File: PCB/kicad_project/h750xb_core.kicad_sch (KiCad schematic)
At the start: 9 parts, among them Q1 Q_NMOS_GSD, SW1 SW_DPST, SW2 SW_DPST

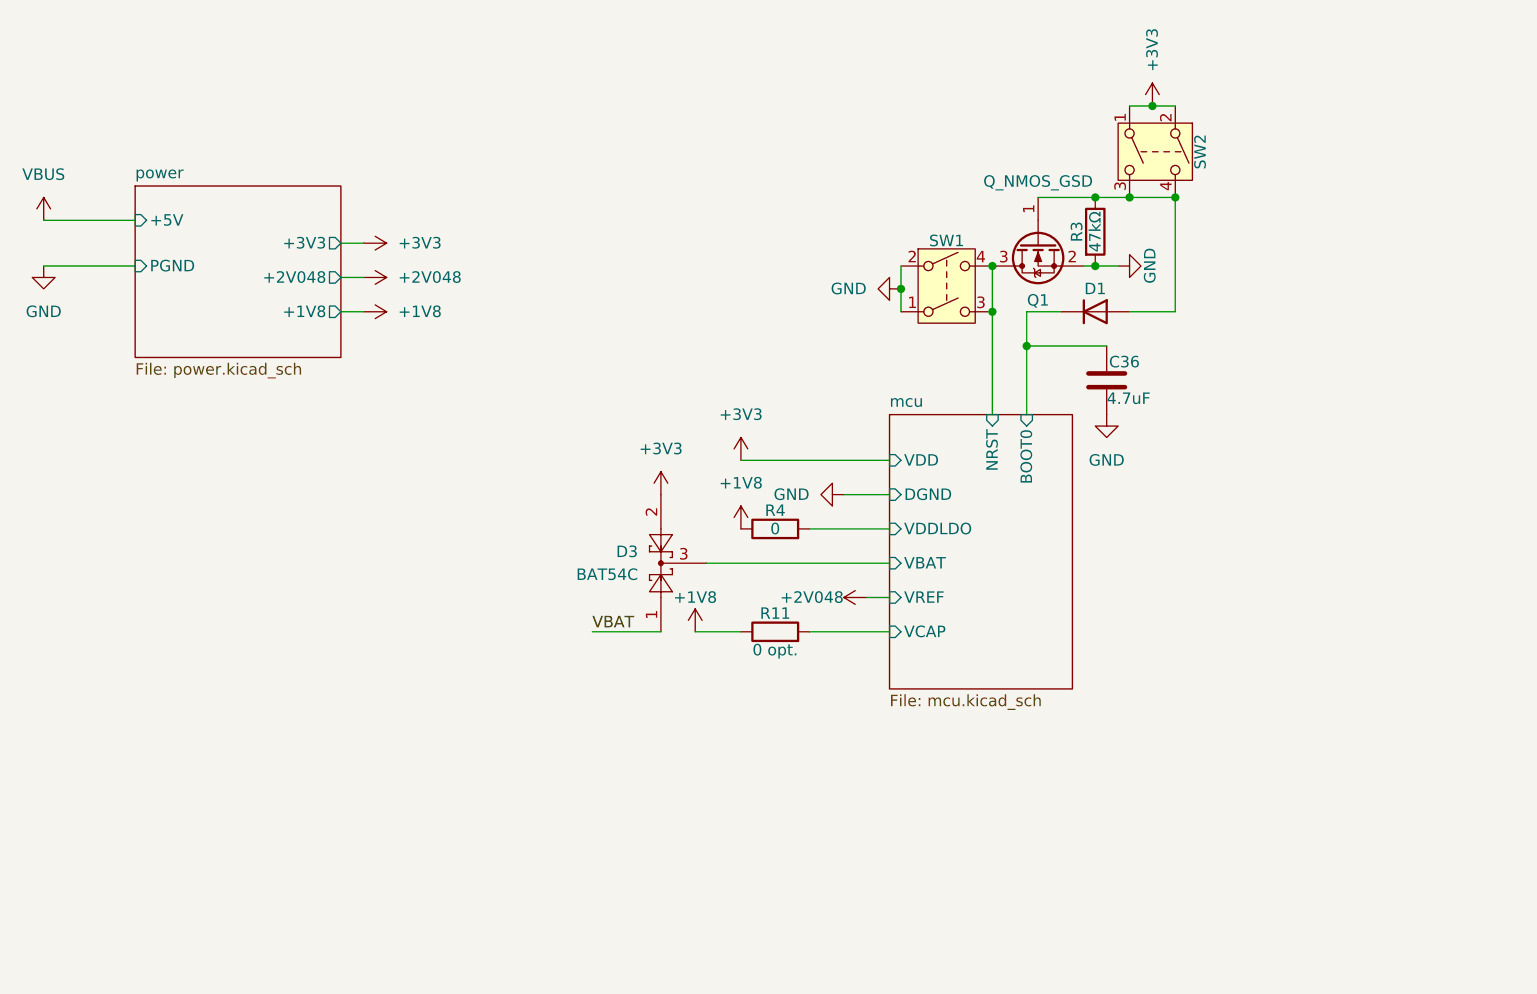
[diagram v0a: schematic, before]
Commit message: 完成了SDRAM和QSPI的走线，QSPI做了网络等长匹配（两根复用线未连接以用于准确计算线长）
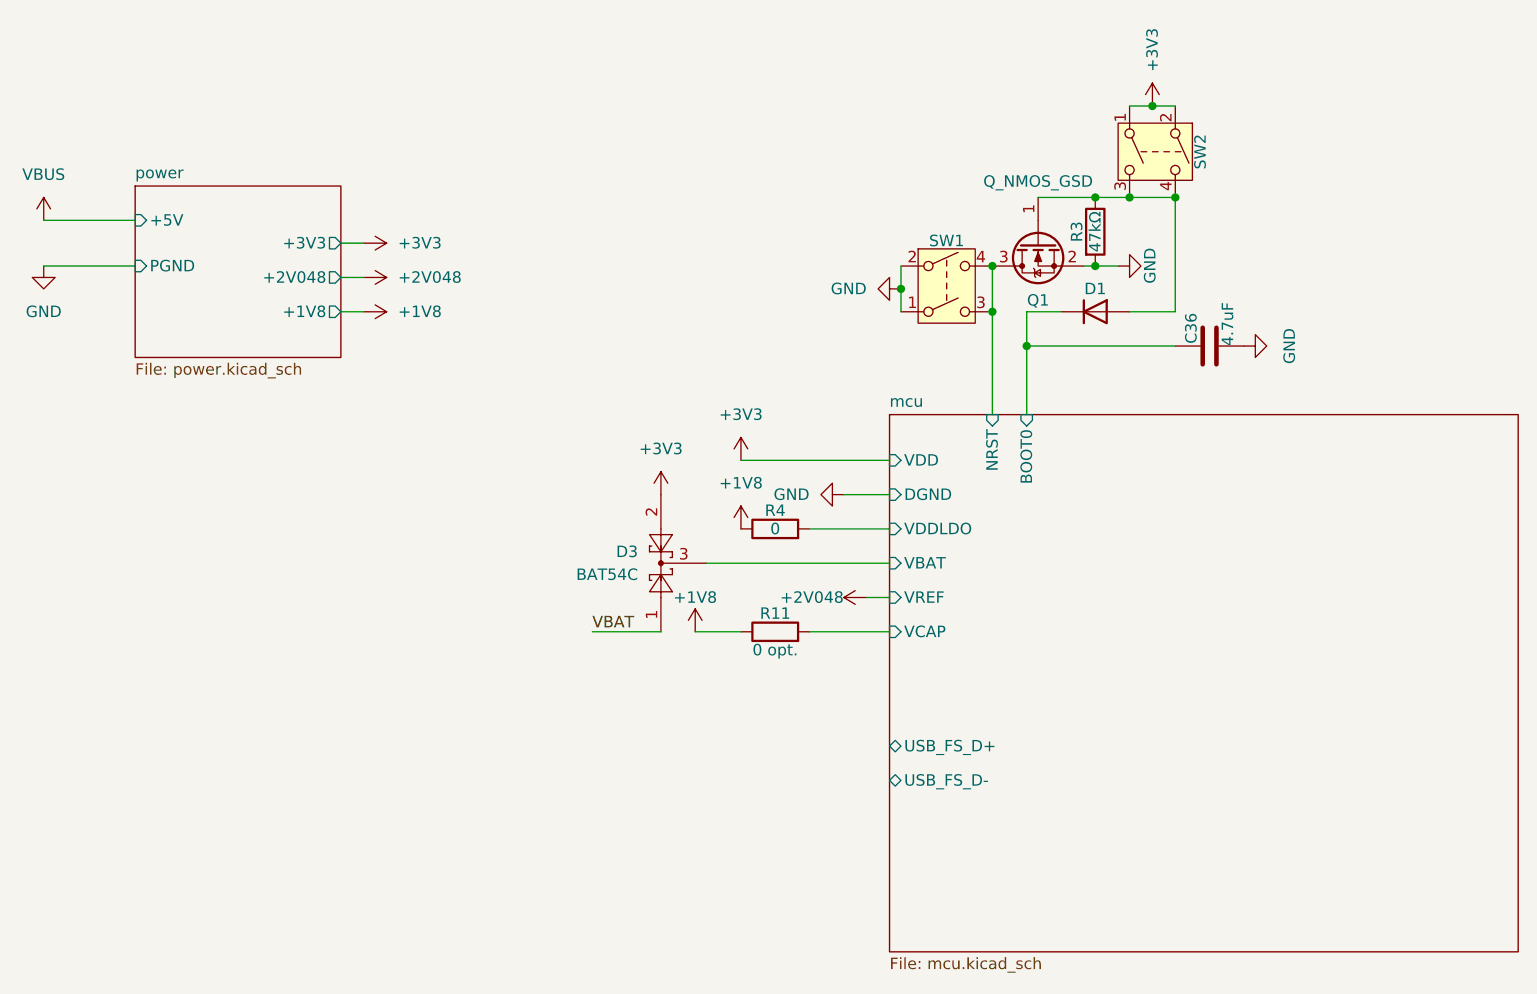
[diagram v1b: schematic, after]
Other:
- sheet mcu ports: added USB_FS_D+, USB_FS_D-; removed none
- moved on the sheet: C36
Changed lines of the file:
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@@
+	(wire
+		(pts
+			(xy 147.32 53.34) (xy 163.83 53.34)
+		)
+		(stroke
+			(width 0)
+			(type default)
+		)
+	)
 	(wire
 		(pts
@@
 		(pts
 			(xy 147.32 53.34) (xy 147.32 60.96)
-		)
-		(stroke
-			(width 0)
-			(type default)
-		)
-	)
-	(wire
-		(pts
-			(xy 156.21 53.34) (xy 147.32 53.34)
 		)
 		(stroke
@@
 	(symbol
 		(lib_id "power:GND")
-		(at 156.21 60.96 0)
+		(at 171.45 53.34 90)
 		(unit 1)
 		(exclude_from_sim no)
@@
 		(fields_autoplaced yes)
 		(property "Reference" "#PWR05"
-			(at 156.21 67.31 0)
+			(at 177.8 53.34 0)
 			(effects
 				(font
@@
 		)
 		(property "Value" "GND"
-			(at 156.21 66.04 0)
+			(at 176.53 53.34 0)
 			(effects
 				(font
@@
 		)
 		(property "Footprint" ""
-			(at 156.21 60.96 0)
+			(at 171.45 53.34 0)
 			(effects
 				(font
@@
 		)
 		(property "Datasheet" ""
-			(at 156.21 60.96 0)
+			(at 171.45 53.34 0)
 			(effects
 				(font
@@
 		)
 		(property "Description" "Power symbol creates a global label with name \"GND\" , ground"
-			(at 156.21 60.96 0)
+			(at 171.45 53.34 0)
 			(effects
 				(font
@@
 	(symbol
 		(lib_id "Device:C")
-		(at 156.21 57.15 0)
+		(at 167.64 53.34 90)
 		(unit 1)
 		(exclude_from_sim no)
@@
 		(dnp no)
 		(property "Reference" "C36"
-			(at 156.464 55.118 0)
+			(at 165.608 53.086 0)
 			(effects
 				(font
@@
 		)
 		(property "Value" "4.7uF"
-			(at 156.21 59.182 0)
+			(at 169.672 53.34 0)
 			(effects
 				(font
@@
 		)
 		(property "Footprint" "Capacitor_SMD:C_0402_1005Metric"
-			(at 157.1752 60.96 0)
+			(at 171.45 52.3748 0)
 			(effects
 				(font
@@
 		)
 		(property "Datasheet" "~"
-			(at 156.21 57.15 0)
+			(at 167.64 53.34 0)
 			(effects
 				(font
@@
 		)
 		(property "Description" "Unpolarized capacitor"
-			(at 156.21 57.15 0)
+			(at 167.64 53.34 0)
 			(effects
 				(font
@@
 	(sheet
 		(at 132.08 60.96)
-		(size 20.32 30.48)
+		(size 69.85 59.69)
 		(fields_autoplaced yes)
 		(stroke
@@
 		)
 		(property "Sheetfile" "mcu.kicad_sch"
-			(at 132.08 92.0246 0)
+			(at 132.08 121.2346 0)
 			(effects
 				(font
@@
 			(effects
 				(font
+					(size 1.27 1.27)
+				)
+				(justify left)
+			)
+		)
+		(pin "USB_FS_D-" bidirectional
+			(at 132.08 101.6 180)
+			(effects
+				(font
+					(size 1.27 1.27)
+				)
+				(justify left)
+			)
+		)
+		(pin "USB_FS_D+" bidirectional
+			(at 132.08 97.79 180)
+			(effects
+				(font

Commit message: 铺铜，增加BTB
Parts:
- removed C36: 4.7uF, Capacitor_SMD:C_0402_1005Metric, symbol Device:C
- removed D1: D, Diode_SMD:D_SOD-323, symbol Device:D
- removed Q1: Q_NMOS_GSD, Package_TO_SOT_SMD:SOT-23, symbol Device:Q_NMOS_GSD
- removed R3: 47kΩ, Resistor_SMD:R_0402_1005Metric, symbol Device:R
- removed SW1, SW2: SW_DPST, my:SW_SMD_4P-L4.2-W3.2-P2.15-LS4.6-1, symbol Switch:SW_DPST
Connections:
- net VBAT renamed ex_VBAT
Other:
- sheet mcu ports: added none; removed USB_FS_D+, USB_FS_D-
